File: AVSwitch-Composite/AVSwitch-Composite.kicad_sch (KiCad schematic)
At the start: 7 parts, among them J1 Conn_01x35_Pin, U1 SN74CBT3244PW

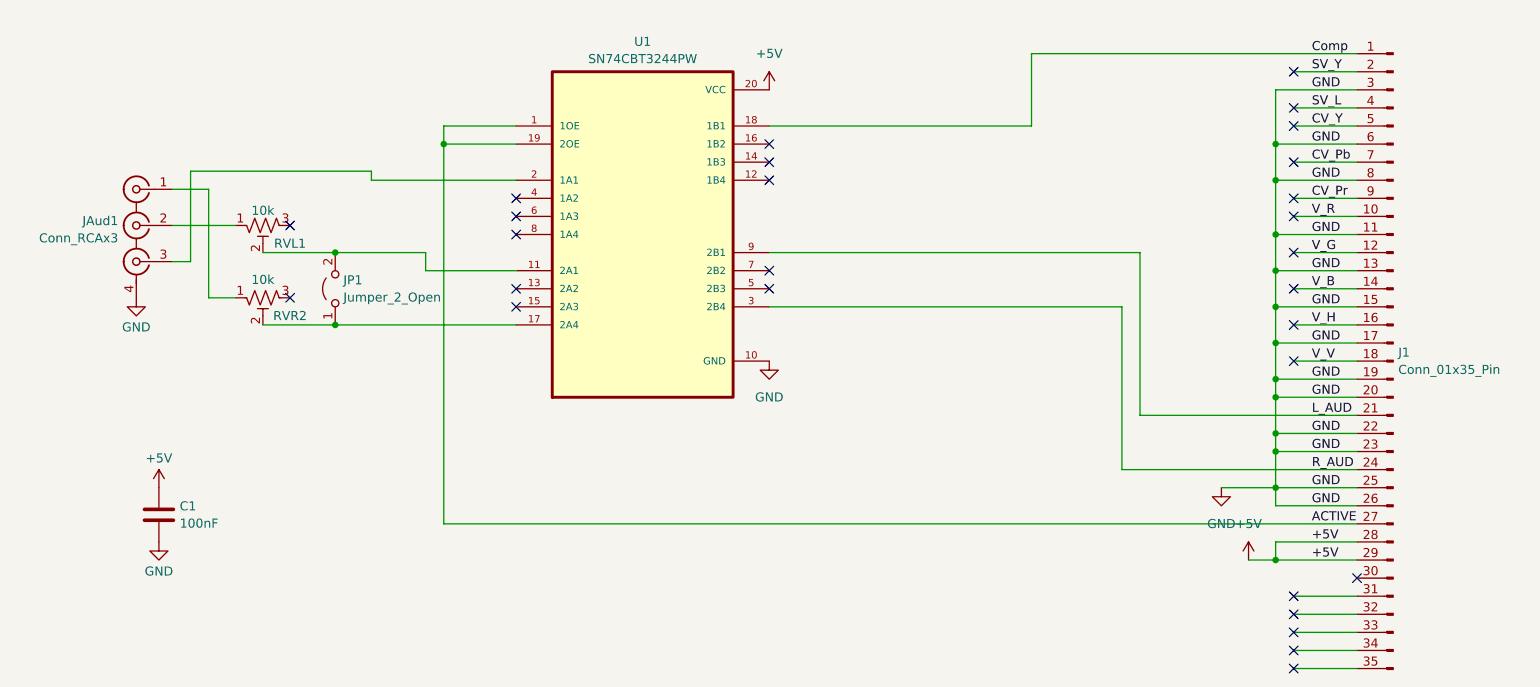
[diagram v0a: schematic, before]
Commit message: Add files via upload
New version with better footprint and ground isolation.
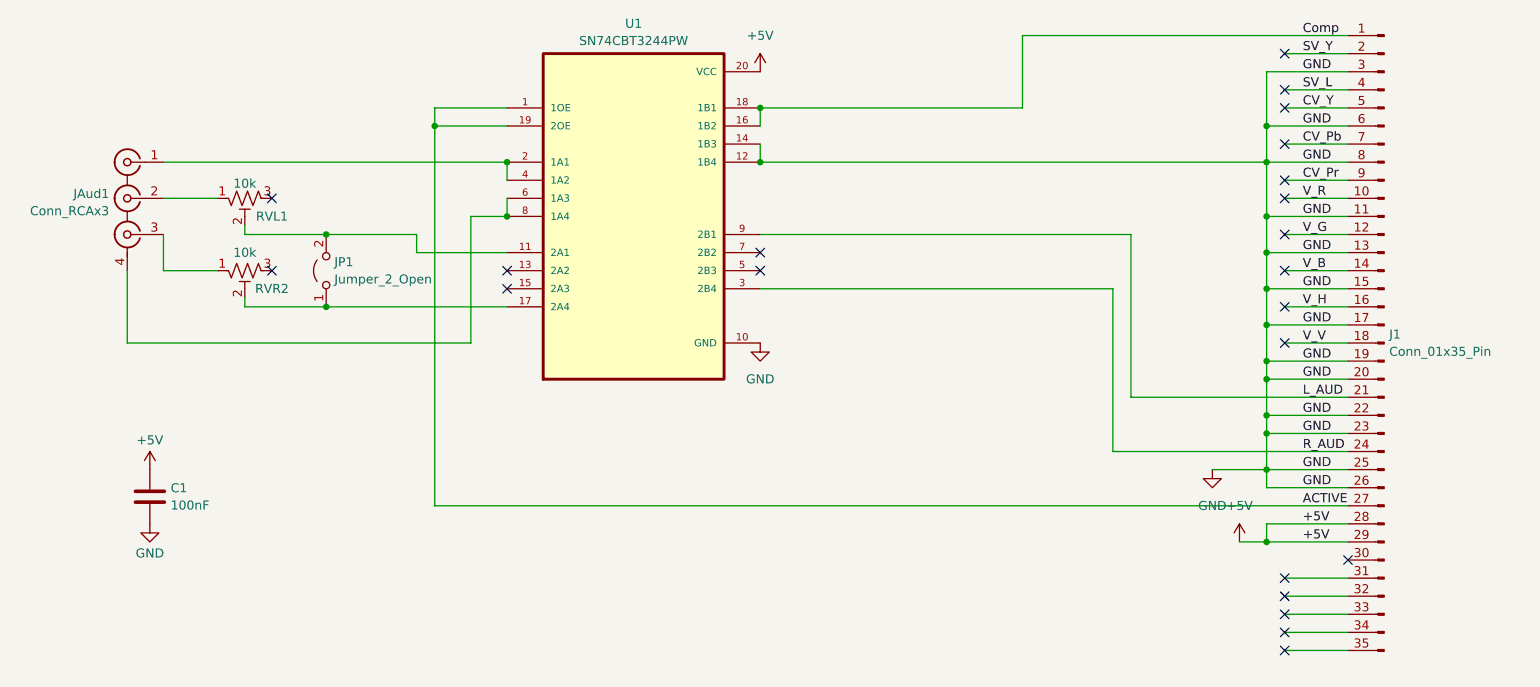
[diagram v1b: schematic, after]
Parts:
- U1: footprint Package_SO:TSSOP-20_4.4x6.5mm_P0.65mm -> Package_SO:SOIC-20W_7.5x12.8mm_P1.27mm
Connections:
- net Comp: now also U1.16 (1B2)
- net GND: now also U1.12 (1B4), U1.14 (1B3); no longer JAud1.4 (GND)
- net at RVR2.1: now also JAud1.3 (IN1); no longer JAud1.1 (IN1)
- net at U1.2 (1A1): now also JAud1.1 (IN1), U1.4 (1A2); no longer JAud1.3 (IN1)
- net at U1.6 (1A3): now also JAud1.4 (GND), U1.8 (1A4)
- no-connect marks 28 -> 22
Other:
- moved on the sheet: C1, J1, JAud1, JP1, RVL1, RVR2, U1
